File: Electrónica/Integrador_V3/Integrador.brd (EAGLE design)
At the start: 47.8 x 24.8 mm, 12 parts, among them J1 22-27-2031-03, U1 OPA4228PA, X3 SMA-142-0711-821/826, X4 SMA-142-0711-821/826

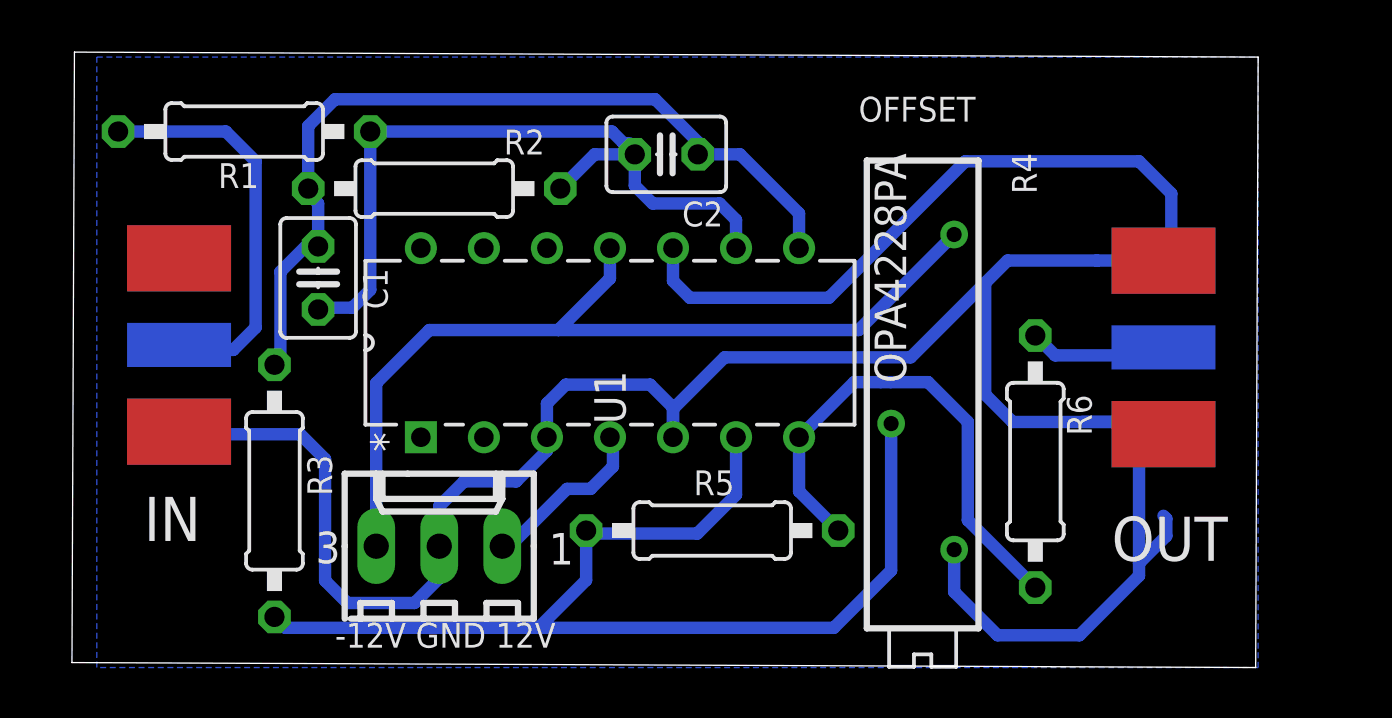
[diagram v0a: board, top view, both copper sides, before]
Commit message: Integrador con 5.2 cm de largo y usando el opa4228
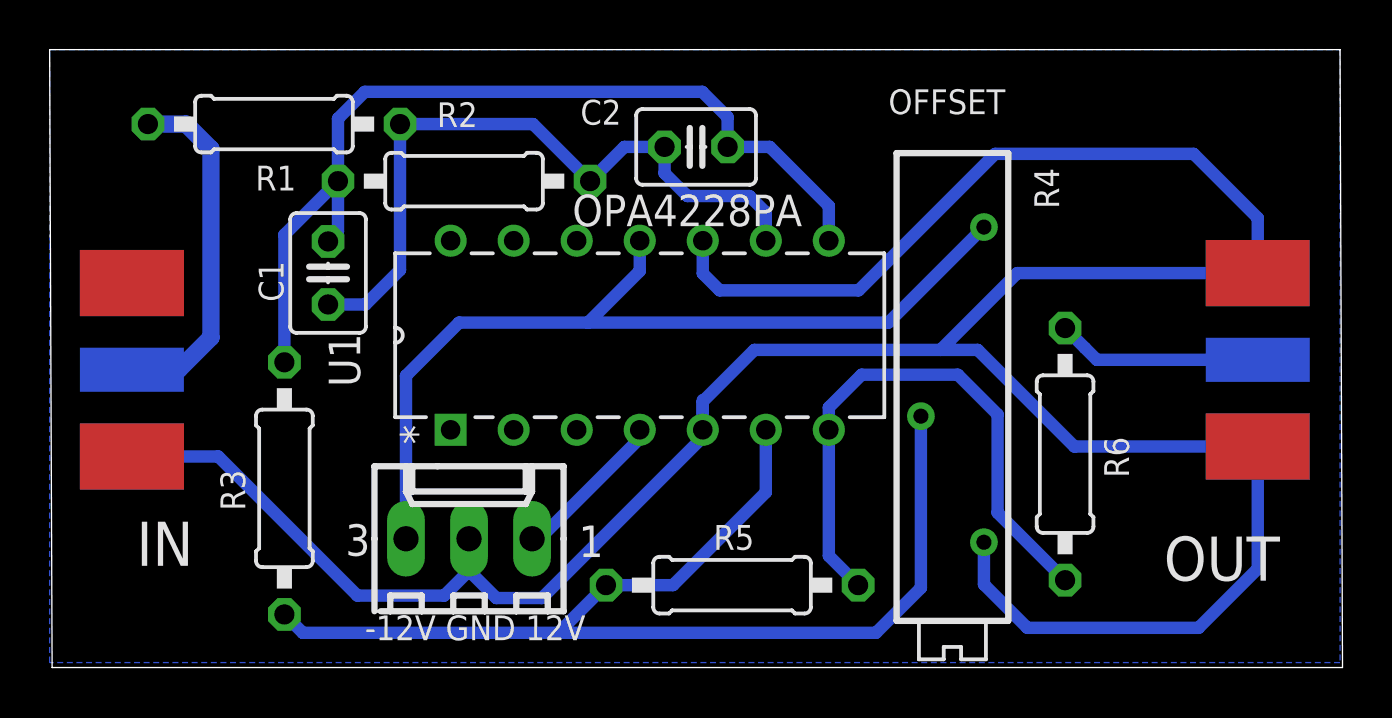
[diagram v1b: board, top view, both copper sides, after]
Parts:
- moved X4 3.83 mm to (50.7, 12.4)
- moved R5 2.34 mm to (27.4, 3.32)
- moved X3 2.15 mm to (1.10, 12.0)
- moved R4 1.24 mm to (36.3, 10.1)
- moved R6 1.24 mm to (40.8, 8.60)
- moved J1 1.24 mm to (16.8, 5.19)
- moved R2 1.24 mm to (16.6, 19.6)
- moved C2 1.24 mm to (25.9, 21.0)
- moved U1 1.24 mm to (31.3, 17.2)
- moved R1 1.24 mm to (8.94, 21.9)
- moved C1 0.45 mm to (11.1, 15.9)
- moved R3 0.41 mm to (9.36, 7.22)
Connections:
- removed net N$10: U1.1
- removed net N$11: U1.2
- net GND: no longer U1.3
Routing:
- net N$7: track 5.18 -> 8.29 mm
- net N$1: track 17.4 -> 14.3 mm
- net GND: track 117.7 -> 120.6 mm
- net OUTC: track 34.6 -> 37.5 mm
- net OUTB: track 20.6 -> 23.5 mm
- net INC-: track 30.8 -> 28.5 mm
- net INB-: track 45.7 -> 46.9 mm
- net 12V: track 7.02 -> 6.46 mm
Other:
- board size 47.8 x 24.8 mm -> 52.1 x 24.9 mm
